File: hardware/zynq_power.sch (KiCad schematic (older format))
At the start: 68 parts, among them U201 xc7z030sbg485

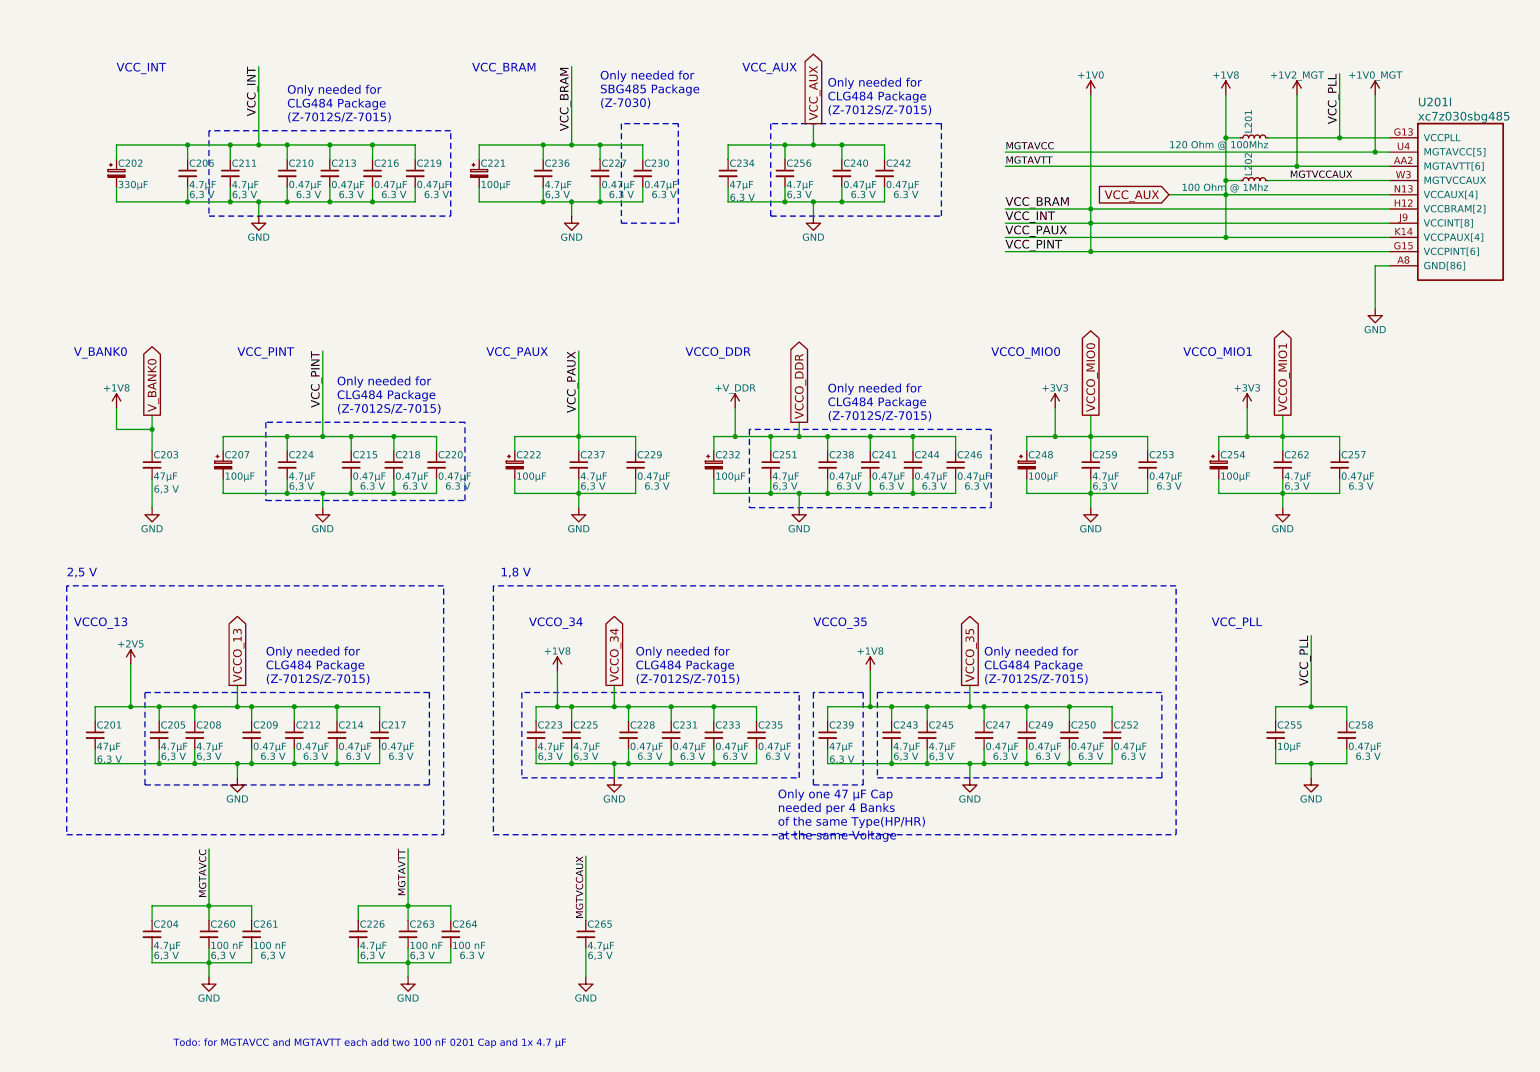
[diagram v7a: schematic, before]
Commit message: PS Clock, Reset Button, Cam Levelshifters and big 1.0 V Cap placed.
Improved some Footprints and library Symbols.

Also though about Chassis Ground.
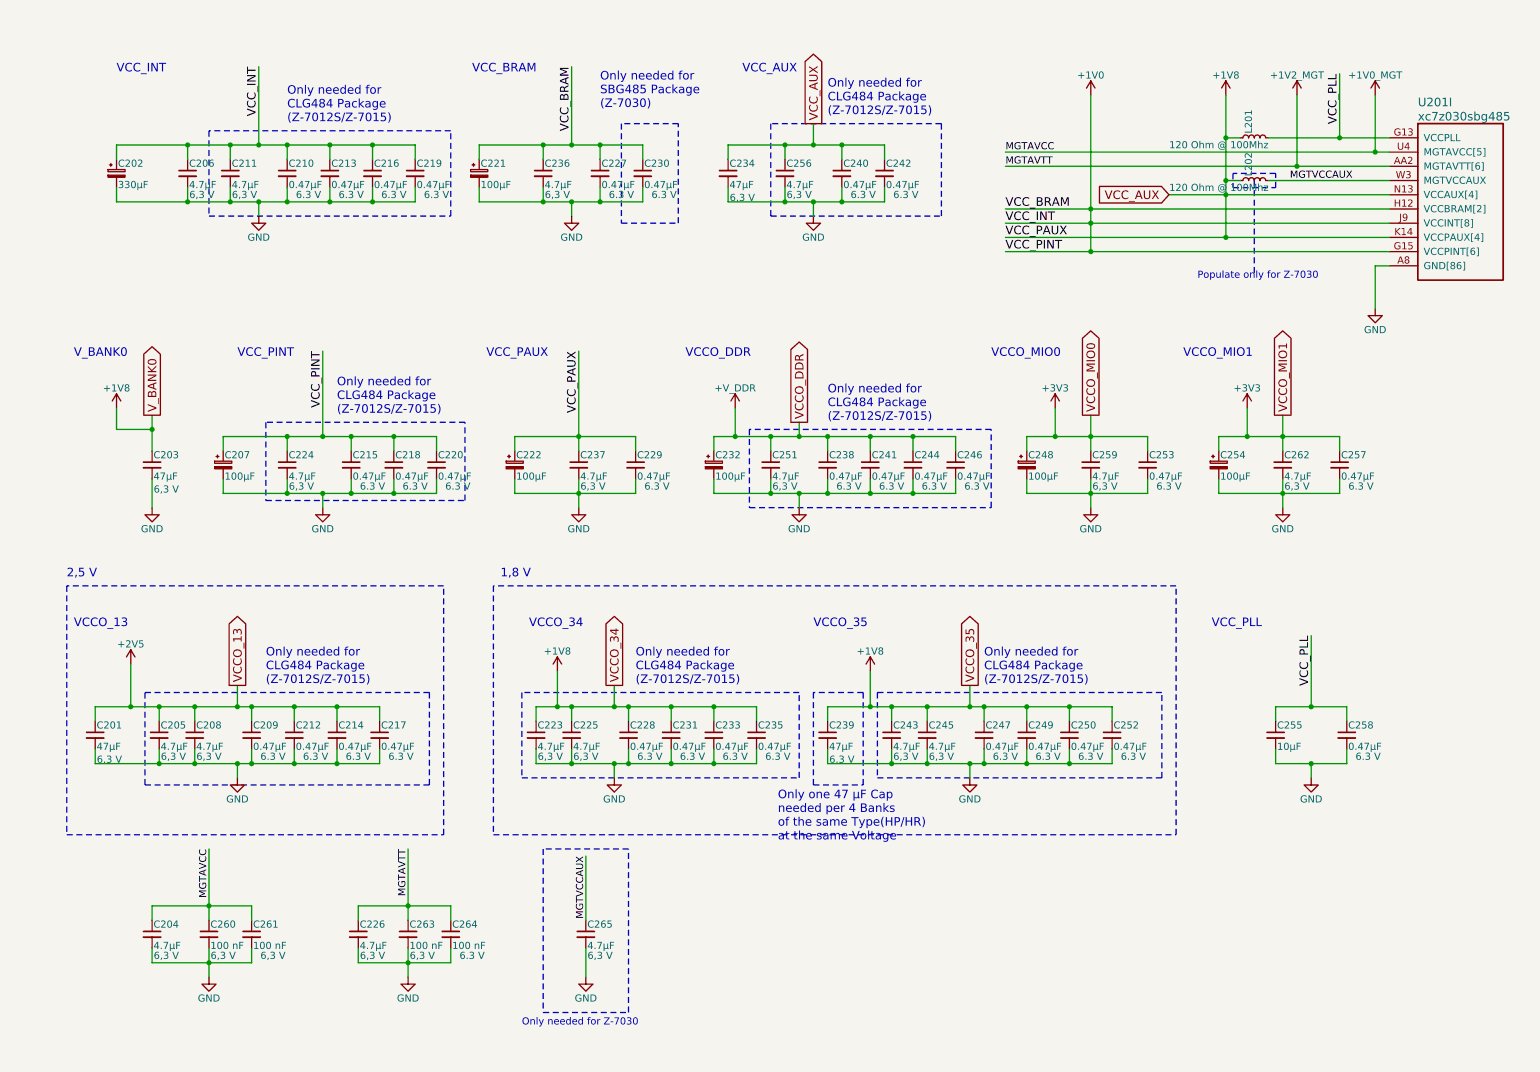
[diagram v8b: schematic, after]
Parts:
- C202: footprint (none) -> footprints:C7343-21_KEMET-V_10.22x5.6mm; Populate for CLG484(Z-7012s/Z-7015) (none) -> 1; Populate for SBGA485(Z-7030) (none) -> 1
- C265: Populate for CLG484(Z-7012s/Z-7015) 1 -> DNP; Populate for SBGA485(Z-7030) 1 -> POPULATE
- L201: footprint Inductors_SMD:L_0603 -> Inductor_SMD:L_0603_1608Metric
- L202: value 100 Ohm @ 1Mhz -> 120 Ohm @ 100Mhz; footprint (none) -> Inductor_SMD:L_0603_1608Metric; Digikey (none) -> 490-3996-1-ND; MFG Name (none) -> Murata Electronics North America; MFG Part Num (none) -> BLM18SG121TN1D; Populate for CLG484(Z-7012s/Z-7015) (none) -> DNP; Populate for SBGA485(Z-7030) (none) -> POPULATE; Populated (none) -> 1; Source (none) -> SPEC
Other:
- note added: "Only needed for Z-7030"
- note added: "Populate only for Z-7030"
- note removed: "Todo: for MGTAVCC and MGTAVTT each add two 100 nF 0201 Cap and 1x 4.7 µF"
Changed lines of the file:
@@
 F 0 "C202" H 960 1570 50  0000 L CNN
 F 1 "330µF" H 960 1420 50  0000 L CNN
-F 2 "" H 950 1500 50  0001 C CNN
+F 2 "footprints:C7343-21_KEMET-V_10.22x5.6mm" H 950 1500 50  0001 C CNN
 F 3 "http://www.kemet.com/docfinder?Partnumber=T520" H 950 1500 50  0001 C CNN
 F 4 "KEMET" H 950 1500 60  0001 C CNN "MFG Name"
@@
 F 8 "CAP TANT POLY 330UF 2.5V 2917, ESR < 50mOhm" H 950 1500 60  0001 C CNN "Description"
 F 9 "SPEC" H 950 1500 60  0001 C CNN "Source"
+F 10 "1" H 950 1500 50  0001 C CNN "Populate for SBGA485(Z-7030)"
+F 11 "1" H 950 1500 50  0001 C CNN "Populate for CLG484(Z-7012s/Z-7015)"
 	1    950  1500
 	1    0    0    -1
-$EndComp
-$Comp
-L Device:L_Small L202
-U 1 1 5AE1F2BF
-P 8950 1550
-F 0 "L202" H 8980 1590 50  0000 L CNN
-F 1 "100 Ohm @ 1Mhz" V 8900 1450 50  0000 L CNN
-F 2 "" H 8950 1550 50  0001 C CNN
-F 3 "" H 8950 1550 50  0001 C CNN
-	1    8950 1550
-	0    -1   -1   0
 $EndComp
 $Comp
@@
 F 0 "L201" H 8980 1290 50  0000 L CNN
 F 1 "120 Ohm @ 100Mhz" V 8900 1150 50  0000 L CNN
-F 2 "Inductors_SMD:L_0603" H 8950 1250 50  0001 C CNN
+F 2 "Inductor_SMD:L_0603_1608Metric" H 8950 1250 50  0001 C CNN
 F 3 "https://www.murata.com/en-us/products/productdata/8796738650142/ENFA0003.pdf" H 8950 1250 50  0001 C CNN
 F 4 "Murata Electronics North America" H 8950 1250 60  0001 C CNN "MFG Name"
@@
 Text Label 3000 6250 3    50   ~ 0
 MGTAVTT
-Text Notes 1350 7650 0    50   ~ 0
-Todo: for MGTAVCC and MGTAVTT each add two 100 nF 0201 Cap and 1x 4.7 µF
 $Comp
 L Device:C_Small C260
@@
 F 8 "CAP CER 4.7UF 6.3V X7R 0603" H 4250 6850 60  0001 C CNN "Description"
 F 9 "SPEC" H 4250 6850 60  0001 C CNN "Source"
-F 10 "1" H 4250 6850 60  0001 C CNN "Populate for SBGA485(Z-7030)"
-F 11 "1" H 4250 6850 60  0001 C CNN "Populate for CLG484(Z-7012s/Z-7015)"
+F 10 "POPULATE" H 4250 6850 60  0001 C CNN "Populate for SBGA485(Z-7030)"
+F 11 "DNP" H 4250 6850 60  0001 C CNN "Populate for CLG484(Z-7012s/Z-7015)"
 F 12 "6,3 V" H 4350 6700 50  0000 C CNN "Voltage"
 	1    4250 6850
@@
 Wire Wire Line
 	4250 6300 4250 6750
+$Comp
+L Device:L_Small L202
+U 1 1 5BC0494E
+P 8950 1550
+F 0 "L202" H 8980 1590 50  0000 L CNN
+F 1 "120 Ohm @ 100Mhz" V 8900 1450 50  0000 L CNN
+F 2 "Inductor_SMD:L_0603_1608Metric" H 8950 1550 50  0001 C CNN
+F 3 "https://www.murata.com/en-us/products/productdata/8796738650142/ENFA0003.pdf" H 8950 1550 50  0001 C CNN
+F 4 "Murata Electronics North America" H 8950 1550 60  0001 C CNN "MFG Name"
+F 5 "BLM18SG121TN1D" H 8950 1550 60  0001 C CNN "MFG Part Num"
+F 6 "490-3996-1-ND" H 8950 1550 60  0001 C CNN "Digikey"
+F 7 "1" H 8950 1550 60  0001 C CNN "Populated"
+F 8 "SPEC" H 8950 1550 60  0001 C CNN "Source"
+F 9 "POPULATE" H 8950 1550 50  0001 C CNN "Populate for SBGA485(Z-7030)"
+F 10 "DNP" H 8950 1550 50  0001 C CNN "Populate for CLG484(Z-7012s/Z-7015)"
+	1    8950 1550
+	0    -1   -1   0
+$EndComp
+Text Notes 8550 2250 0    50   ~ 0
+Populate only for Z-7030
+Wire Notes Line
+	8800 1500 8800 1600
+Wire Notes Line
+	8800 1600 9100 1600
+Wire Notes Line
+	9100 1600 9100 1500
+Wire Notes Line
+	9100 1500 8800 1500
+Wire Notes Line
+	8950 1550 8950 2200
+Wire Notes Line
+	3950 7400 4550 7400
+Wire Notes Line
+	4550 7400 4550 6250
+Wire Notes Line
+	4550 6250 3950 6250
+Wire Notes Line
+	3950 6250 3950 7400
+Text Notes 3800 7500 0    50   ~ 0
+Only needed for Z-7030
 $EndSCHEMATC
